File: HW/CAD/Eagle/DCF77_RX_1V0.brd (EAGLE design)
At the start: 98.4 x 89.5 mm, 41 parts, among them IC251 LMH6645MF, IC271 LMH6645MF, J131 2SK3557, Q211 QT26V-77.000k, X101 PHOENIX_1990067_1X8X2MM50_PTS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, X391 PHOENIX_1990067_1X8X2MM50_PTS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

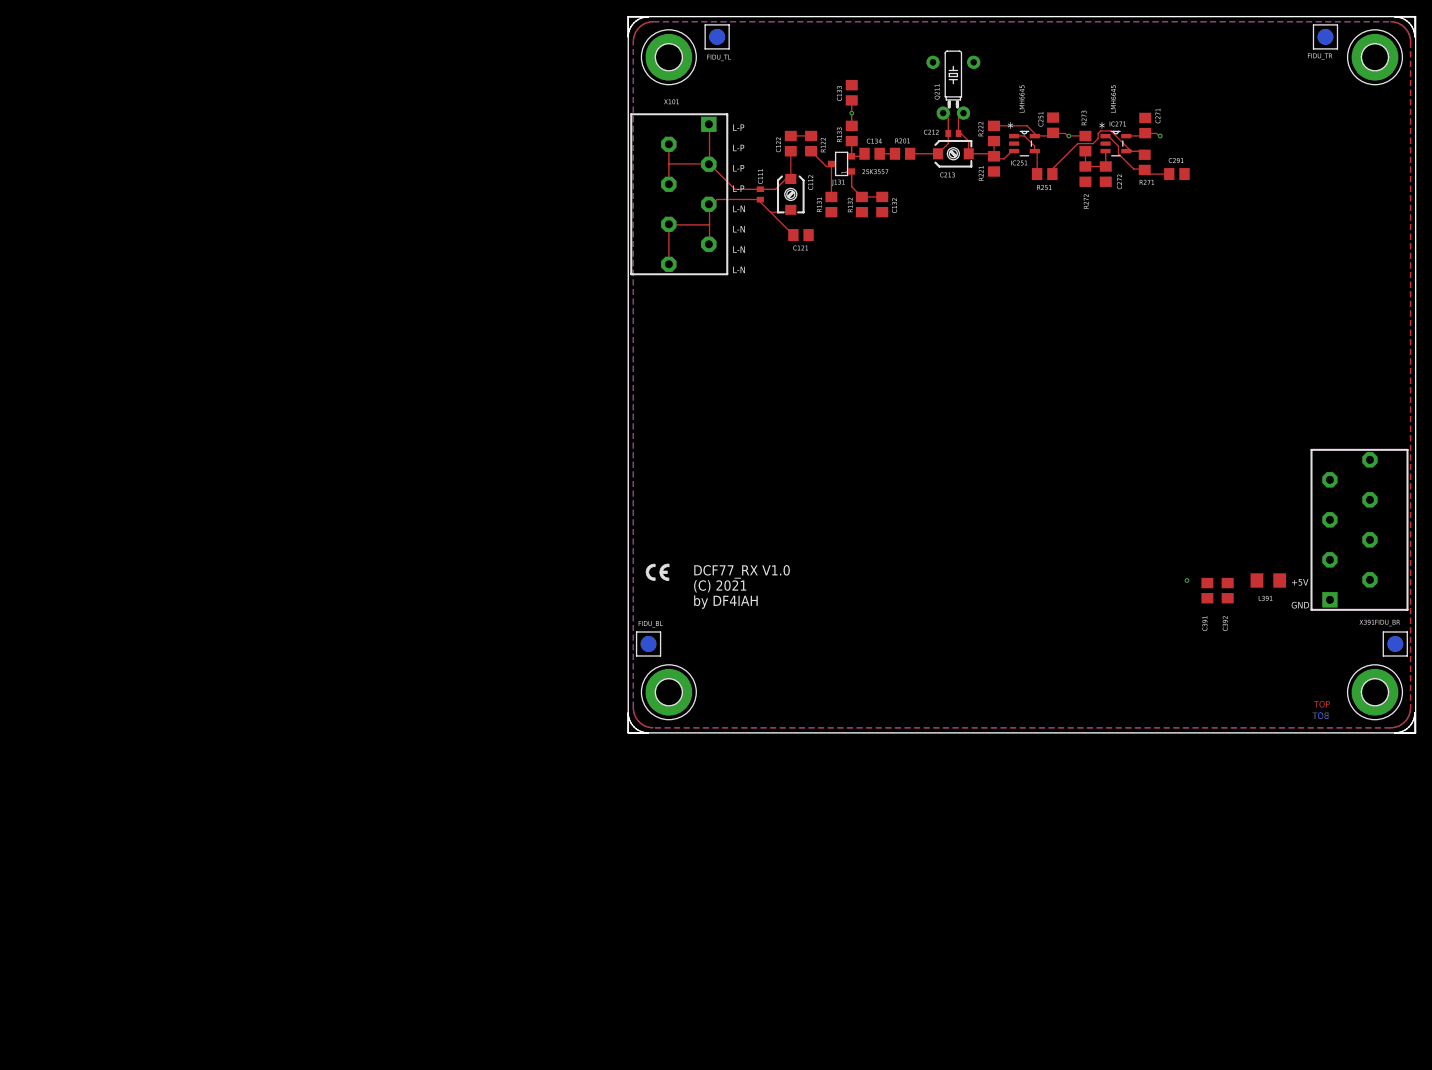
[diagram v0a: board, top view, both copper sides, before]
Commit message: HW - Eagle - adaptions from simulation made, layout to do
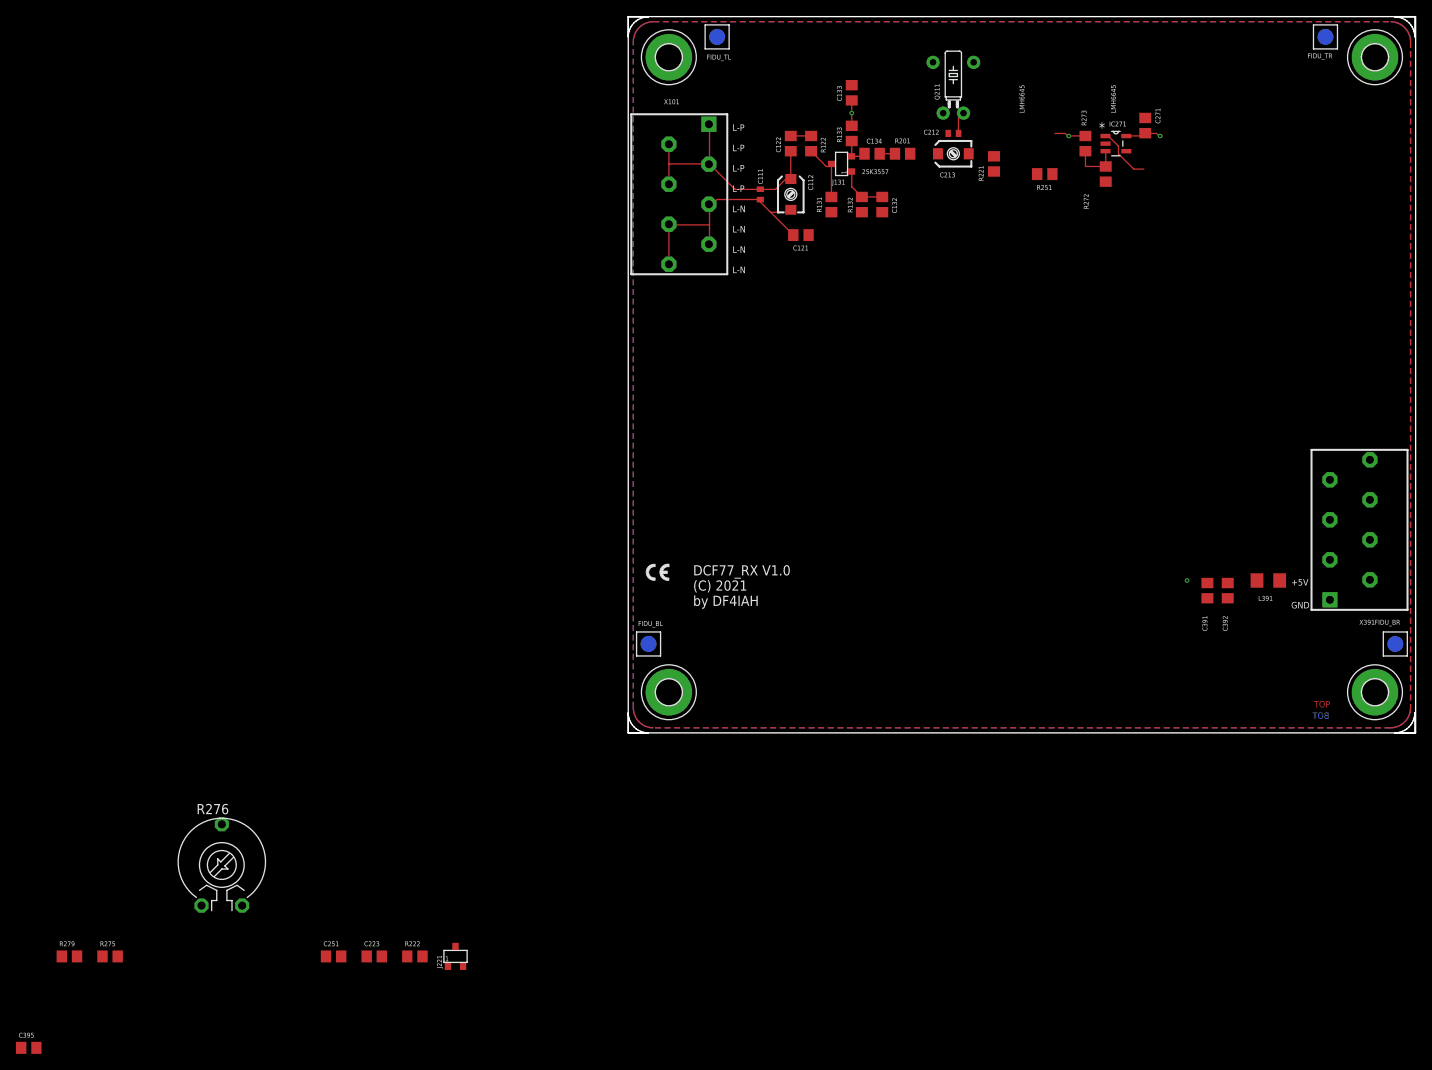
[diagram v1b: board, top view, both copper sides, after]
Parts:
- removed C272: 10nF, df4iah_rcl:C0805
- removed C291: 100nF, df4iah_rcl:C0805
- removed IC251: LMH6645MF, df4iah_opamp:SOT-23-5
- removed R271: 100kR, df4iah_rcl:R0805
- added C223: 10uF, df4iah_rcl:C0805
- added C395: 47pF, df4iah_rcl:C0805
- added J221: 2SK3557, df4iah_jfet:SOT23-3
- added R275, R279: 1kR, df4iah_rcl:R0805
- added R276: 100kR, df4iah_rcl:PT-10
- C111: value 6.8pF -> 10pF
- C121, C122: value 1nF -> 10nF
- C132: value 1uF -> 2.2uF
- C133: value 4.7uF -> 10uF
- C134: value 100nF -> 2.2nF
- C212: value 5.6pF -> 1.5pF
- C251: value 10uF -> 100nF
- R201: value 68kR -> 10kR
- R221: value 100kR -> 1MR
- R222: value 100kR -> 390R
- R251: value 270R -> 1kR
- R272, R273: value 100kR -> 1kR
- moved C251 137.4 mm to (-36.8, -27.9), turned to 0 degrees
- moved R222 125.8 mm to (-26.7, -27.9), turned to 0 degrees
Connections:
- removed net N211: C212.1, C213.CROT, Q211.1, R201.2
- new net N$2: Q211.1, R201.2
- new net N222: C251.1, J221.P$1, R222.2
- new net N275: R275.2, R276.1
- net +5V: now also C223.1, J221.P$2; no longer C251.1, IC251.5, R222.2
- net DIG_OUT: now also C395.1, R279.2, X391.7; no longer C291.2, X391.8
- net GND: now also C212.2, C213.CSTAT, C223.2, C395.2, R222.1, X391.3, X391.6, X391.8; no longer C251.2, C272.2, IC251.2
- net N221: now also C212.1, C213.CROT, J221.P$3; no longer C212.2, C213.CSTAT, IC251.3, R222.1
- net N251: now also C251.2; no longer IC251.1, IC251.4
- net N271: now also R276.3, R279.1; no longer C291.1, R271.2
- net N272: now also IC271.3, R272.2, R273.1; no longer IC271.4, R251.2, R271.1
- net N273: now also IC271.4, R251.2, R275.1; no longer C272.1, IC271.3, R272.2, R273.1
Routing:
- net N221: track 14.5 -> 2.80 mm
- net N272: track 17.0 -> 6.35 mm
- net N211: track 9.38 -> 0.00 mm
- net +5V: track 20.3 -> 11.6 mm
- net N251: track 6.91 -> 0.00 mm
- net N273: track 6.39 -> 0.00 mm
- net N271: track 10.5 -> 7.06 mm

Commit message: HW - Eagle - Hardware ready for the PCB house V1.0
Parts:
- removed FIDU_BL, FIDU_BR, FIDU_TL, FIDU_TR: (no value), df4iah_fiducial:FIDUCIAL_MARK_1MM
- removed IC271: LMH6645MF, df4iah_opamp:SOT-23-5
- added U271: LMH6645MF, df4iah_opamp:SOT-23-5
- moved C395 148.8 mm to (58.4, 26.7), turned to 90 degrees
- moved R279 125.7 mm to (49.5, 11.4), turned to 90 degrees
- moved R275 110.9 mm to (39.4, 10.2), turned to 180 degrees
- moved C251 87.1 mm to (38.1, 16.5), turned to 270 degrees
- moved C223 84.9 mm to (40.6, 16.5), turned to 270 degrees
- moved R276 84.8 mm to (30.5, 7.62), turned to 270 degrees
- moved J221 78.5 mm to (39.4, 21.6)
- moved R222 78.0 mm to (35.6, 19.1), turned to 90 degrees
- moved C271 65.0 mm to (43.7, 14.3), turned to 180 degrees
- moved R251 58.5 mm to (39.4, 12.7)
- moved R273 58.0 mm to (47.0, 16.5)
- moved R272 54.3 mm to (49.5, 16.5), turned to 270 degrees
- moved H1513 53.4 mm to (70.5, 36.2)
- moved Q211 52.1 mm to (38.1, 25.4)
- moved R221 48.3 mm to (44.5, 22.9), turned to 180 degrees
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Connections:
- net N$2 renamed N211
- net +5V: now also U271.5; no longer IC271.5
- net GND: now also U271.2; no longer IC271.2
- net N271: now also U271.1; no longer IC271.1
- net N272: now also U271.3; no longer IC271.3
- net N273: now also U271.4; no longer IC271.4
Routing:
- net DIG_OUT: track 0.00 -> 23.3 mm
- net +5V: track 11.6 -> 28.8 mm, vias 4 -> 3
- net N275: track 0.00 -> 13.0 mm
- net N391: track 0.00 -> 11.3 mm
- net N221: track 2.80 -> 11.1 mm
- net N271: track 7.06 -> 15.3 mm
- net N222: track 0.00 -> 6.08 mm
- net N273: track 0.00 -> 5.51 mm
- net N251: track 0.00 -> 2.99 mm
- net N133: track 3.70 -> 6.31 mm
- net N211: track 0.00 -> 2.06 mm
- net N101: track 31.3 -> 29.9 mm
- net N102: track 30.6 -> 29.4 mm
- removed copper zone on layer 14, net +3V3
- removed copper zone on layer 15, net GND
- removed copper zone on layer 2, net GND
- removed copper zone on layer 3, net GND
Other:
- board size 98.4 x 89.5 mm -> 75.6 x 41.3 mm
- board text removed: "L14"
- board text removed: "L15"
- board text removed: "L2"
- board text removed: "L3"
